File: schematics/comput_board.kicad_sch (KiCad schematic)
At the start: 22 parts

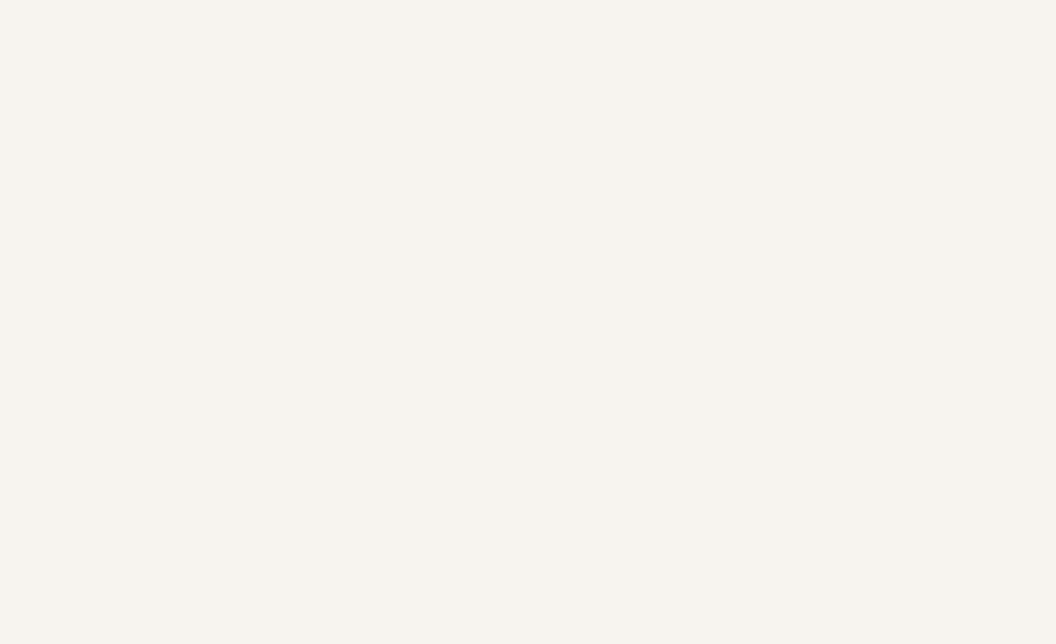
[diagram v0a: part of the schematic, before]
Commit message: added subschimatics
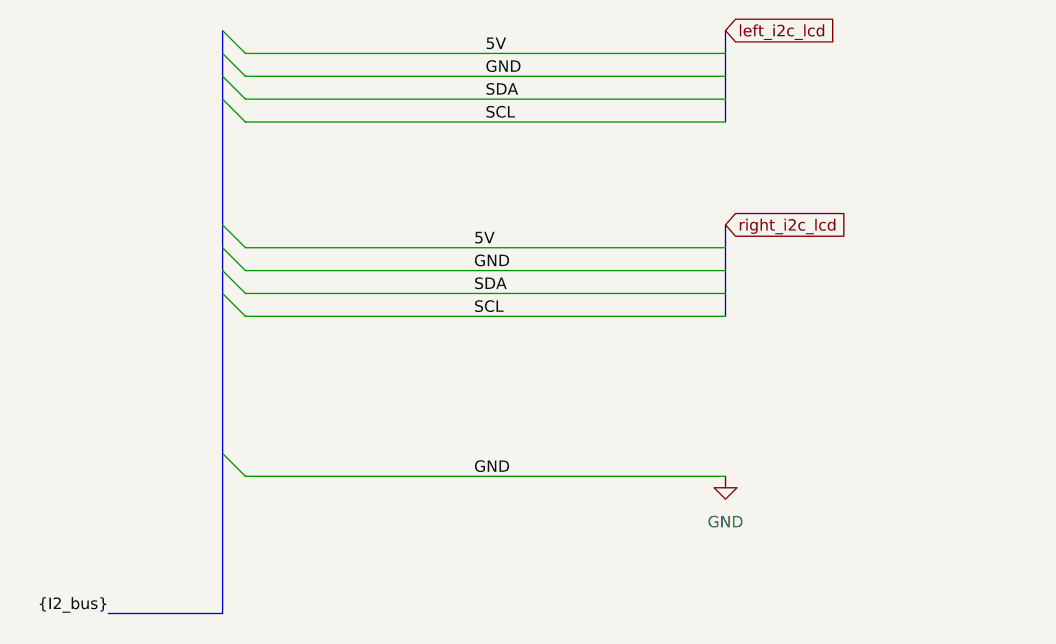
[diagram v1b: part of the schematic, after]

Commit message: mostly done with the sub-schematics
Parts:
- added SW1: SW_Nidec_CAS-120A1, Button_Switch_SMD:Nidec_Copal_CAS-120A, symbol Switch:SW_Nidec_CAS-120A1
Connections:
- new net Car_12V: SW1.2 (B)
- new net switched_12V: SW1.1 (C)

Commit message: added titles to all sheets
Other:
- company: (none) -> wish4snow
- title: (none) -> LED I2C Board
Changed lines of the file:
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@@
 	(generator_version "9.0")
 	(paper "USLetter")
+	(title_block
+		(title "LED I2C Board")
+		(date "2026-01-22")
+		(rev "1")
+		(company "wish4snow")
+	)
 	(junction
 		(at 260.35 119.38)
